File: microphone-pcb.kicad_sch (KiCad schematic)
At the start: 9 parts, among them J1 JST_SUR_1x5_BM05B-SURS-TB-LF-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

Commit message: [#71986] Update connector on sch
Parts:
- removed J1: JST_SUR_1x5_BM05B-SURS-TB-LF-SN, antmicro-footprints:Conn_JST_SUR_1x5_BM05B-SURS-TF-LF-SN, symbol antmicroWire2BoardConnectors:JST_SUR_1x5_BM05B-SURS-TB-LF-SN
- added J1: Conn_FFC_Molex_5019510550, antmicro-footprints:Conn_FFC_Molex_5019510550, symbol antmicroFCCConnectors:Conn_FFC_Molex_5019510550
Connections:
- net BCLK: now also J1.3
- net DATA: now also J1.5
- net GND: now also J1.2, J1.MP
- net VCC: now also J1.1
- net WS: now also J1.4
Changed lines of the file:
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@@
+	)
+	(symbol
+		(lib_id "antmicroFCCConnectors:Conn_FFC_Molex_5019510550")
+		(at 194.31 90.17 0)
+		(unit 1)
+		(exclude_from_sim no)
+		(in_bom yes)
+		(on_board yes)
+		(dnp no)
+		(fields_autoplaced yes)
+		(property "Reference" "J1"
+			(at 203.2 94.615 0)
+			(effects
+				(font
+					(size 1.27 1.27)
+					(thickness 0.15)
+				)
+				(justify left)
+			)
+		)
+		(property "Value" "Conn_FFC_Molex_5019510550"
+			(at 217.17 97.79 0)
+			(effects
+				(font
+					(size 1.27 1.27)
+					(thickness 0.15)
+				)
+				(justify left bottom)
+				(hide yes)
+			)
+		)
+		(property "Footprint" "antmicro-footprints:Conn_FFC_Molex_5019510550"
+			(at 217.17 100.33 0)
+			(effects
+				(font
+					(size 1.27 1.27)
+					(thickness 0.15)
+				)
+				(justify left bottom)
+				(hide yes)
+			)
+		)
+		(property "Datasheet" "https://www.molex.com/content/dam/molex/molex-dot-com/products/automated/en-us/salesdrawingpdf/501/501951/5019510550_sd.pdf?inline"
+			(at 217.17 102.87 0)
+			(effects
+				(font
+					(size 1.27 1.27)
+					(thickness 0.15)
+				)
+				(justify left bottom)
+				(hide yes)
+			)
+		)
+		(property "Description" "Connector FFC/FPC SKT 5 Position 0.5mm Solder Straight Surface Mount T/R"
+			(at 217.17 105.41 0)
+			(effects
+				(font
+					(size 1.27 1.27)
+					(thickness 0.15)
+				)
+				(justify left bottom)
+				(hide yes)
+			)
+		)
+		(property "Manufacturer" "Molex"
+			(at 217.17 107.95 0)
+			(effects
+				(font
+					(size 1.27 1.27)
+					(thickness 0.15)
+				)
+				(justify left bottom)
+				(hide yes)
+			)
+		)
+		(property "MPN" "501951-0550"
+			(at 203.2 97.155 0)
+			(effects
+				(font
+					(size 1.27 1.27)
+					(thickness 0.15)
+				)
+				(justify left)
+			)
+		)
+		(property "Author" "Antmicro"
+			(at 217.17 110.49 0)
+			(effects
+				(font
+					(size 1.27 1.27)
+					(thickness 0.15)
+				)
+				(justify left bottom)
+				(hide yes)
+			)
+		)
+		(property "License" "Apache-2.0"
+			(at 217.17 113.03 0)
+			(effects
+				(font
+					(size 1.27 1.27)
+					(thickness 0.15)
+				)
+				(justify left bottom)
+				(hide yes)
+			)
+		)
+		(pin "2"
+		)
+		(pin "3"
+		)
+		(pin "1"
+		)
+		(pin "MP"
+		)
+		(pin "5"
+		)
+		(pin "4"
+		)
+		(instances
+			(project ""
+				(path "/4a2cf8c5-6ba3-448d-b2e4-bea2166340e3"
+					(reference "J1")
+					(unit 1)
+				)
+			)
+		)
 	)
 	(symbol
@@
 					(unit 1)
 				)
-			)
-		)
-	)
-	(symbol
-		(lib_id "antmicroWire2BoardConnectors:JST_SUR_1x5_BM05B-SURS-TB-LF-SN")
-		(at 194.31 90.17 0)
-		(unit 1)
-		(exclude_from_sim no)
-		(in_bom yes)
-		(on_board yes)
-		(dnp no)
-		(fields_autoplaced yes)
-		(property "Reference" "J1"
-			(at 200.66 95.25 0)
-			(effects
-				(font
-					(size 1.27 1.27)
-					(thickness 0.15)
-				)
-				(justify left)
-			)
-		)
-		(property "Value" "JST_SUR_1x5_BM05B-SURS-TB-LF-SN"
-			(at 214.63 97.79 0)
-			(effects
-				(font
-					(size 1.27 1.27)
-					(thickness 0.15)
-				)
-				(justify left bottom)
-				(hide yes)
-			)
-		)
-		(property "Footprint" "antmicro-footprints:Conn_JST_SUR_1x5_BM05B-SURS-TF-LF-SN"
-			(at 214.63 100.33 0)
-			(effects
-				(font
-					(size 1.27 1.27)
-					(thickness 0.15)
-				)
-				(justify left bottom)
-				(hide yes)
-			)
-		)
-		(property "Datasheet" "https://www.jst.com/wp-content/uploads/2021/09/eSUR-new.pdf"
-			(at 214.63 102.87 0)
-			(effects
-				(font
-					(size 1.27 1.27)
-					(thickness 0.15)
-				)
-				(justify left bottom)
-				(hide yes)
-			)
-		)
-		(property "Description" "Pin Header, Vertical, Wire-to-Board, 0.5 mm, 1 Rows, 5 Contacts, Surface Mount Vertical, SUR"
-			(at 214.63 105.41 0)
-			(effects
-				(font
-					(size 1.27 1.27)
-					(thickness 0.15)
-				)
-				(justify left bottom)
-				(hide yes)
-			)
-		)
-		(property "MPN" " BM05B-SURS-TF(LF)(SN)"
-			(at 200.66 97.79 0)
-			(effects
-				(font
-					(size 1.27 1.27)
-					(thickness 0.15)
-				)
-				(justify left)
-			)
-		)
-		(property "Manufacturer" "JST Automotive Connectors"
-			(at 214.63 107.95 0)
-			(effects
-				(font
-					(size 1.27 1.27)
-					(thickness 0.15)
-				)
-				(justify left bottom)
-				(hide yes)
-			)
-		)
-		(property "Author" "Antmicro"
-			(at 214.63 110.49 0)
-			(effects
-				(font
-					(size 1.27 1.27)
-					(thickness 0.15)
-				)
-				(justify left bottom)
-				(hide yes)
-			)
-		)
-		(property "License" "Apache-2.0"
-			(at 214.63 113.03 0)
-			(effects
-				(font
-					(size 1.27 1.27)
-					(thickness 0.15)
-				)
-				(justify left bottom)
-				(hide yes)
-			)
-		)
-		(pin "2"
-		)
-		(pin "3"
-		)
-		(pin "1"
-		)
-		(pin "4"
-		)
-		(pin "5"
-		)
-		(pin "MP"
-		)
-		(instances
-			(project ""
-				(path "/4a2cf8c5-6ba3-448d-b2e4-bea2166340e3"
-					(reference "J1")
-					(unit 1)
-				)

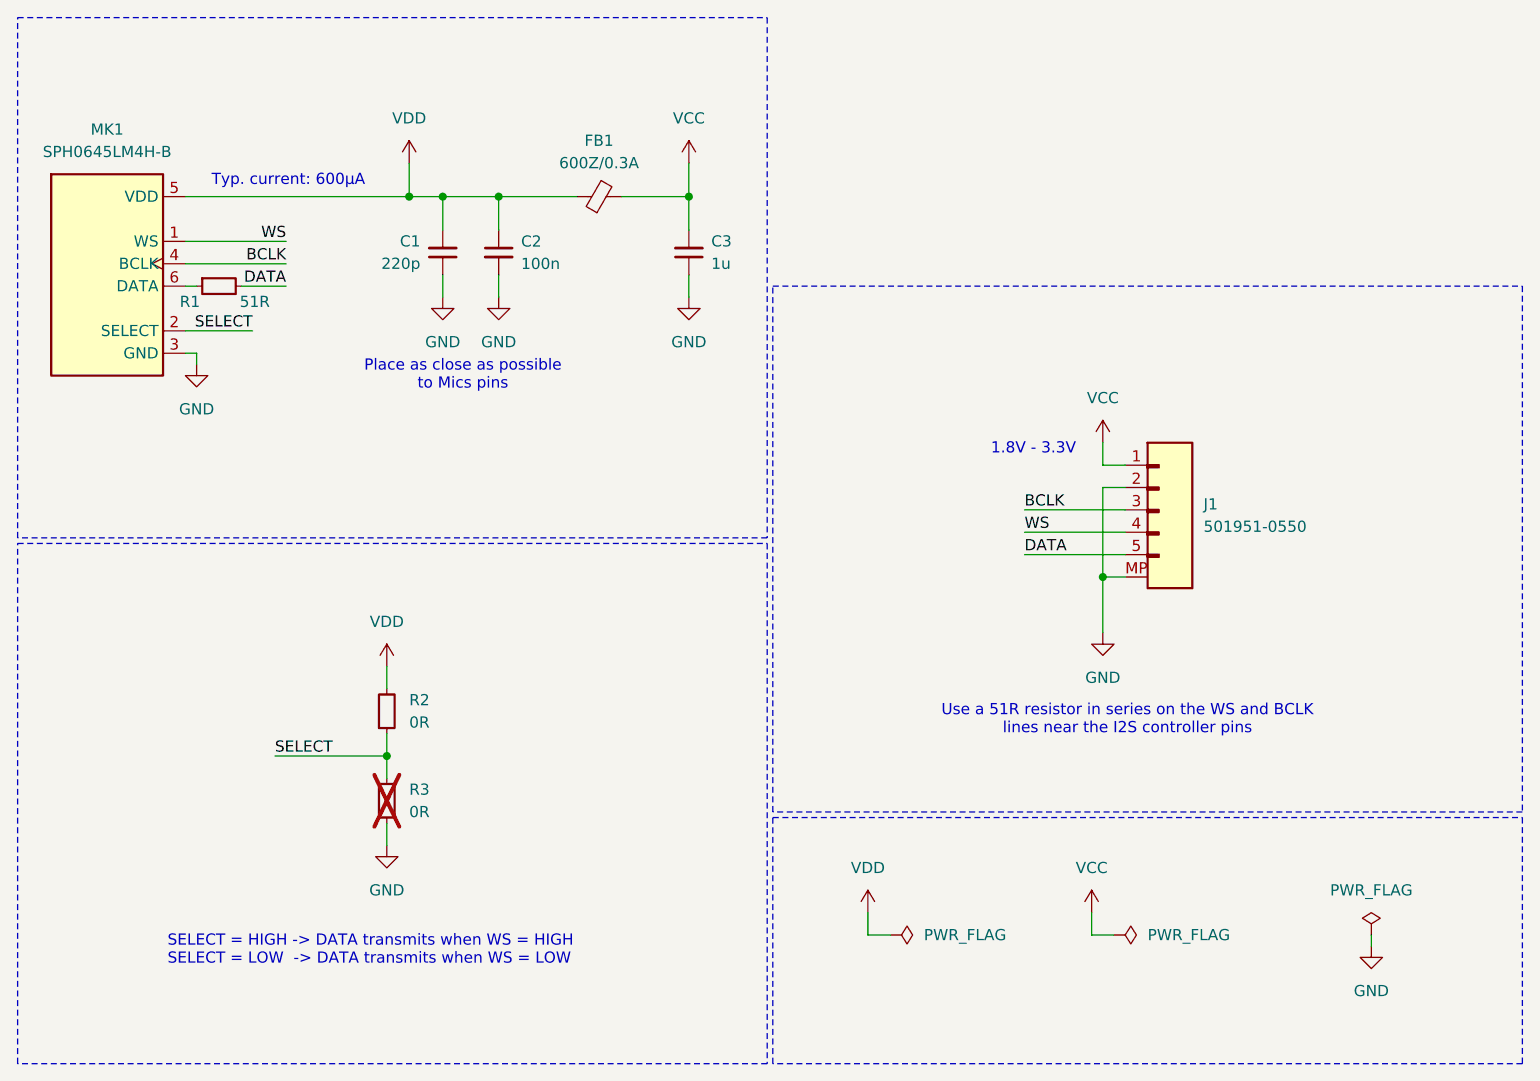
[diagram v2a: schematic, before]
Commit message: [#71986] Add tvs protection
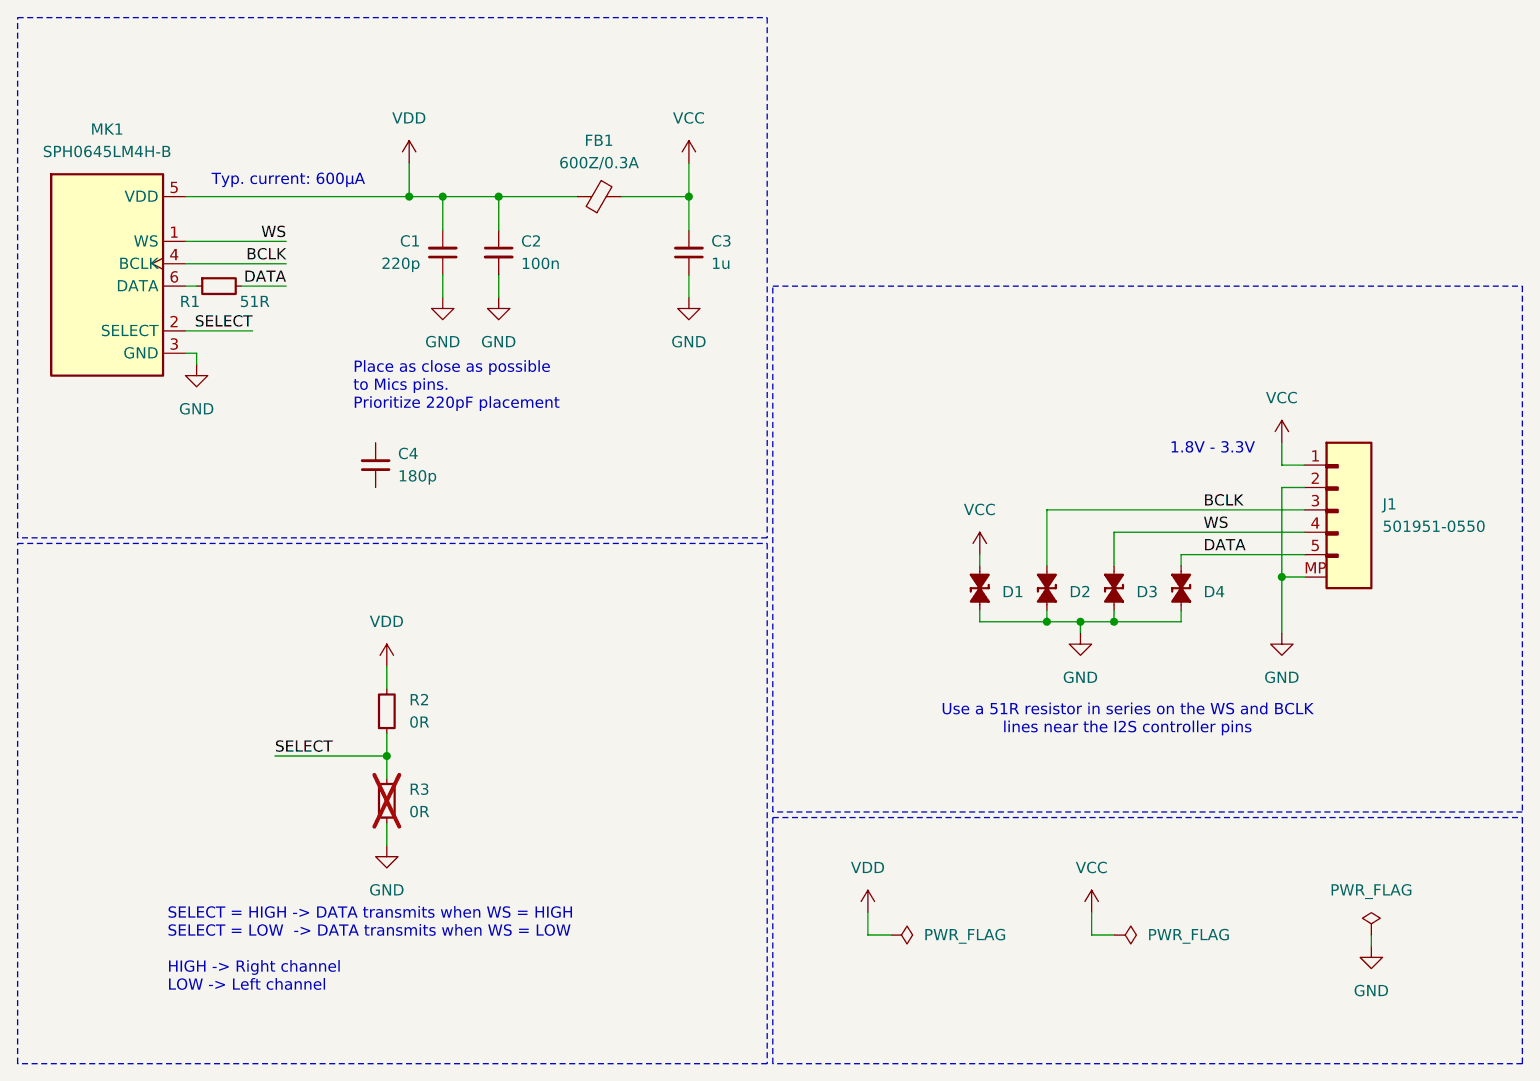
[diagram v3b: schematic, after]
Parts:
- added C4: C_180p_0402, antmicro-footprints:C_0402_1005Metric, symbol antmicroCapacitors0402:C_180p_0402
- added D1, D2, D3, D4: TPD1E0B04_XDFN-2, antmicro-footprints:XDFN-2_1x0.60mm, symbol antmicroTVSDiodes:TPD1E0B04_XDFN-2
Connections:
- net BCLK: now also D2.1 (C)
- net DATA: now also D4.1 (C)
- net GND: now also D1.2 (A), D2.2 (A), D3.2 (A), D4.2 (A)
- net VCC: now also D1.1 (C)
- net WS: now also D3.1 (C)
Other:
- note added: "Place as close as possible to Mics pins. Prioritize 220pF placement"
- note added: "SELECT = HIGH -> DATA transmits when WS = HIGH SELECT = LOW -> DATA transmits when WS = LOW HIGH -> Right channel LOW -> Left channel"
- note removed: "Place as close as possible to Mics pins"
- note removed: "SELECT = HIGH -> DATA transmits when WS = HIGH SELECT = LOW -> DATA transmits when WS = LOW"
- moved on the sheet: J1

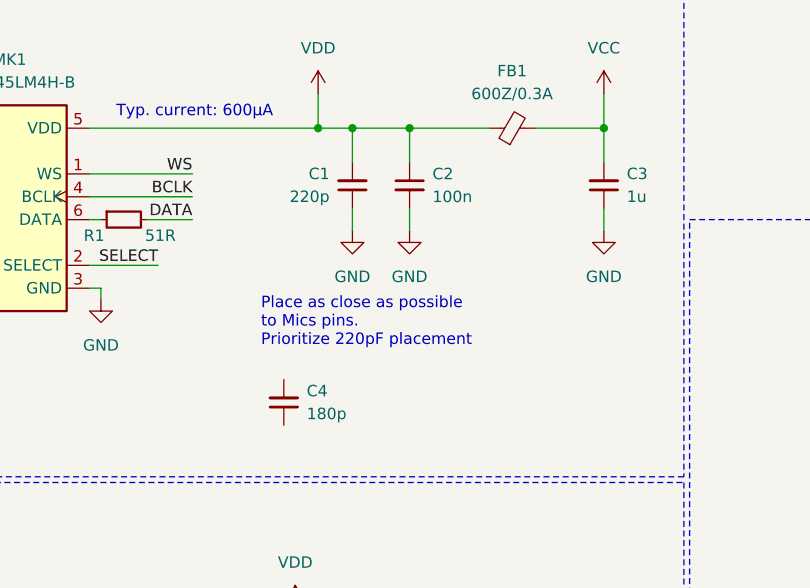
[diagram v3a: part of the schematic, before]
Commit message: [#71986] Replace capacitors with C0G and X8L dielectrics types
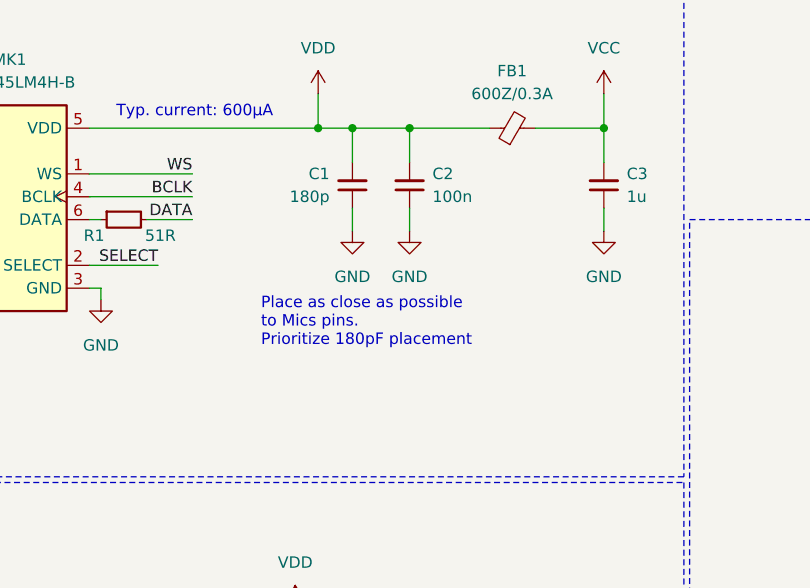
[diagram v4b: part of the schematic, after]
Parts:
- removed C1: C_220p_0402, antmicro-footprints:C_0402_1005Metric, symbol antmicroCapacitors0402:C_220p_0402
- removed C2: C_100n_0402, antmicro-footprints:C_0402_1005Metric, symbol antmicroCapacitors0402:C_100n_0402
- added C2: C_100n_50V_X8L_0402, antmicro-footprints:C_0402_1005Metric, symbol antmicroCapacitors0402:C_100n_50V_X8L_0402
- renumbered C4 to C1
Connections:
- net GND: now also C1.1, C2.1
- net VDD: now also C1.2, C2.2
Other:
- note added: "Place as close as possible to Mics pins. Prioritize 180pF placement"
- note removed: "Place as close as possible to Mics pins. Prioritize 220pF placement"
- moved on the sheet: C1
